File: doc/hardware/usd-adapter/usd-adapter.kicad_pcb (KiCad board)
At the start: 2 copper layers, 14.2 x 25 mm, 2 parts, among them J1 usd-plug, P1 CONN_02X04

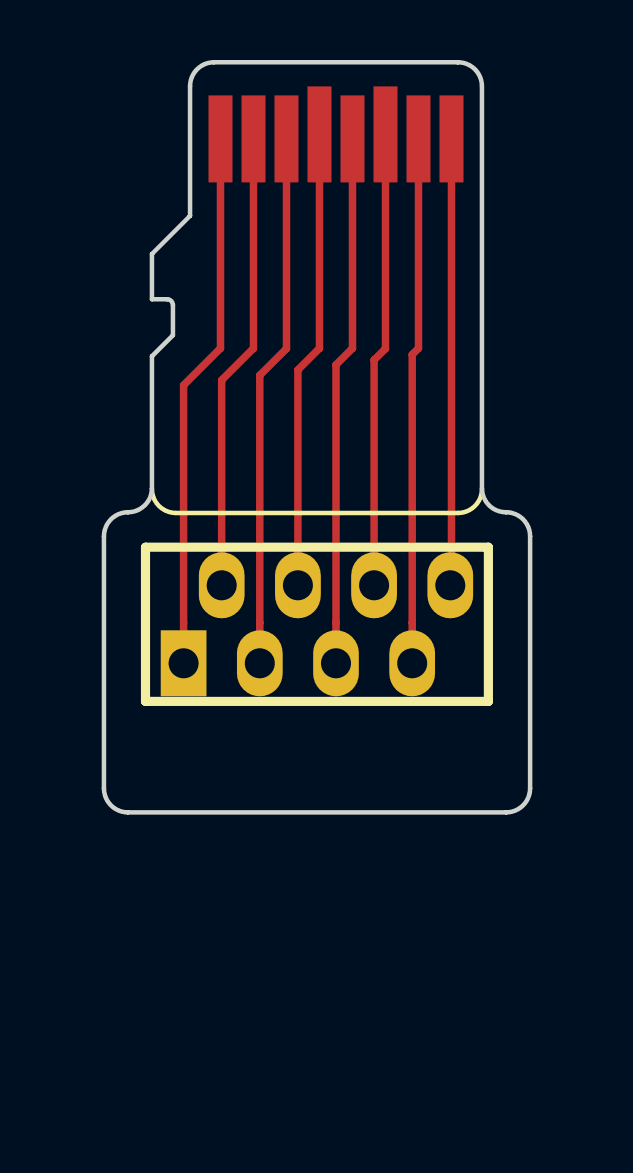
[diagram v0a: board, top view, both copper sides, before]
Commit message: Fix connectors and increase board size on usd-adapter
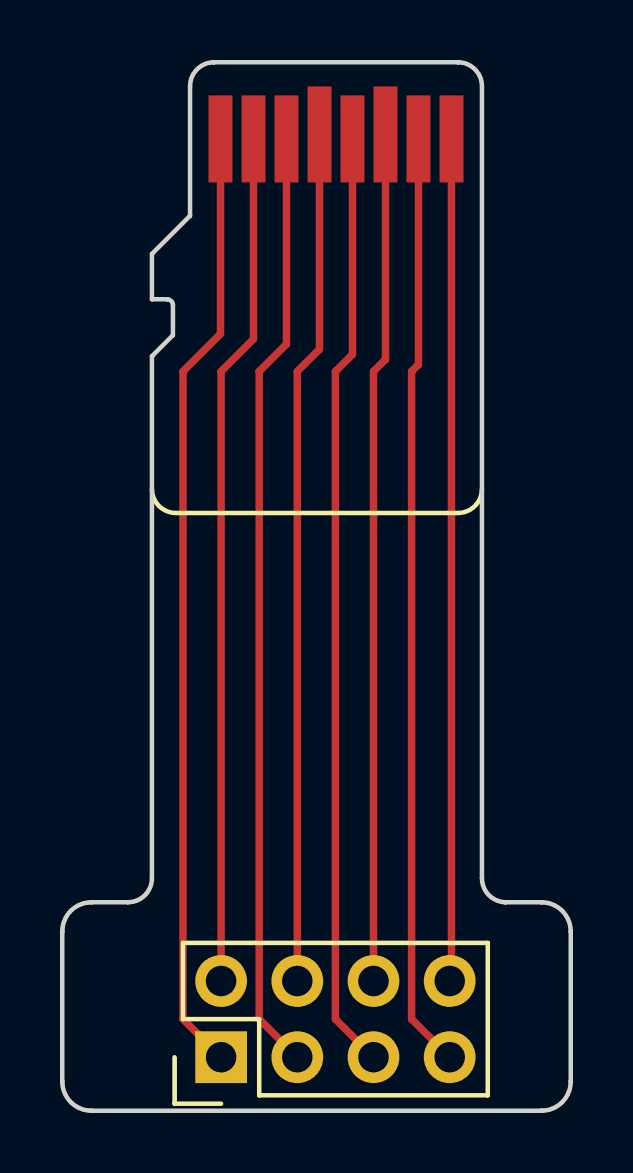
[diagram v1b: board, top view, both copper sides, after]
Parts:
- P1: footprint connectors:strip_2x4_1.27 -> Pin_Headers:Pin_Header_Straight_2x04
- moved P1 13.2 mm to (147.3, 123.2), turned to 90 degrees
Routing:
- net /N5: track 17.7 -> 31.4 mm
- net /N3: track 17.8 -> 31.5 mm
- net /N7: track 17.6 -> 31.2 mm
- net /N1: track 18.0 -> 31.7 mm
- net /N2: track 15.3 -> 28.5 mm
- net /N8: track 14.9 -> 28.1 mm
- net /N6: track 15.2 -> 28.4 mm
- net /N4: track 15.3 -> 28.5 mm
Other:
- board size 14.2 x 25 mm -> 16.9 x 34.9 mm
